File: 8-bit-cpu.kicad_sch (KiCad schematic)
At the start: 24 parts

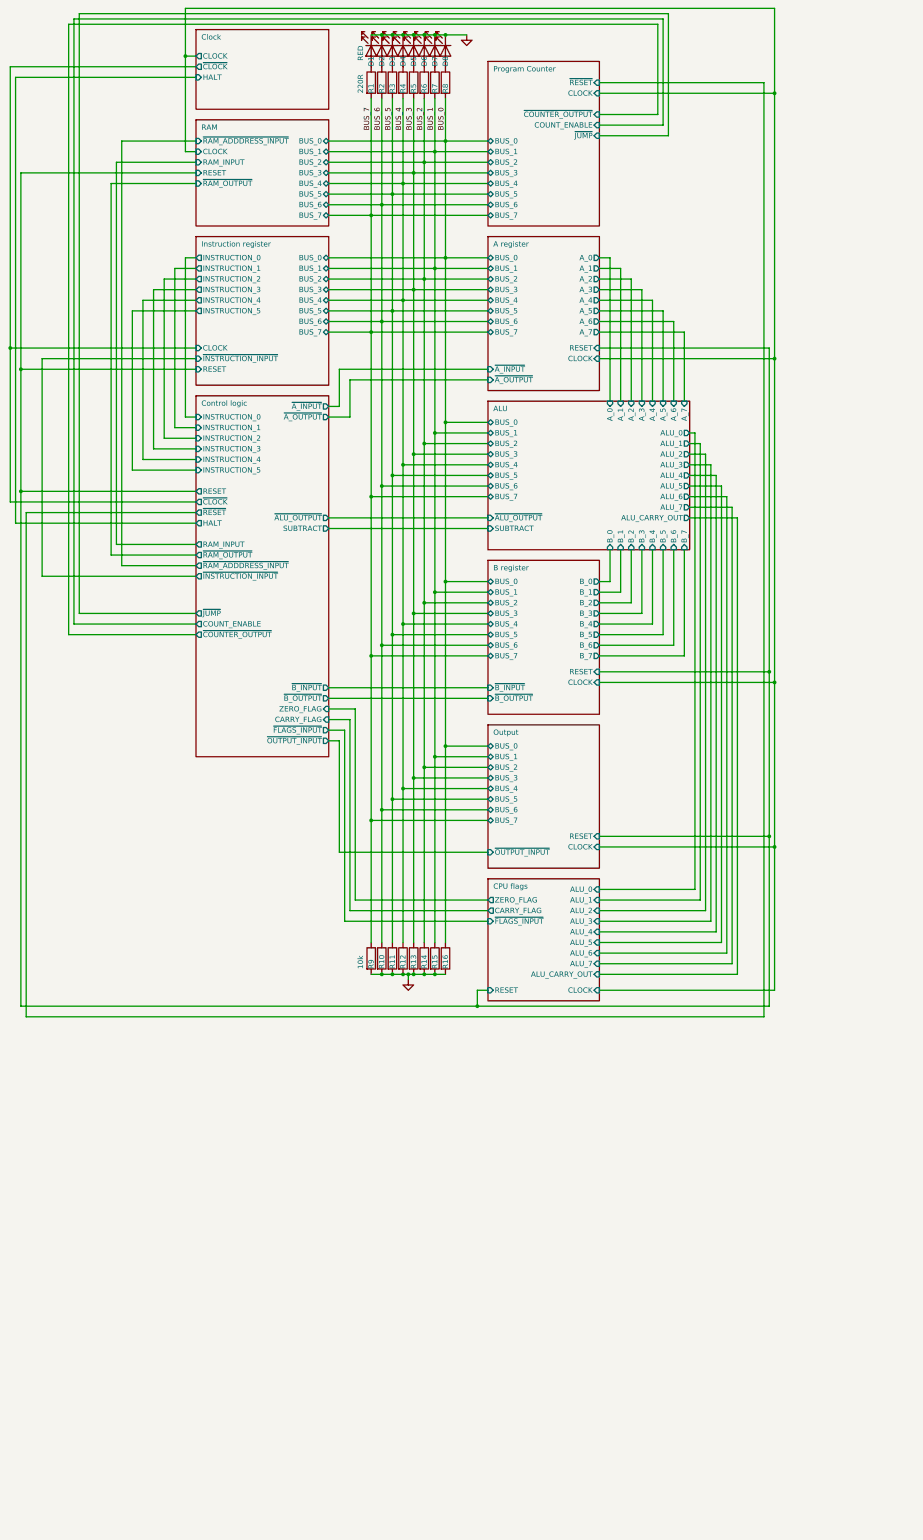
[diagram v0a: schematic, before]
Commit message: added stack and x register.  Added logic for stack_address so ram address 7 gets passes and ram address 8 is high
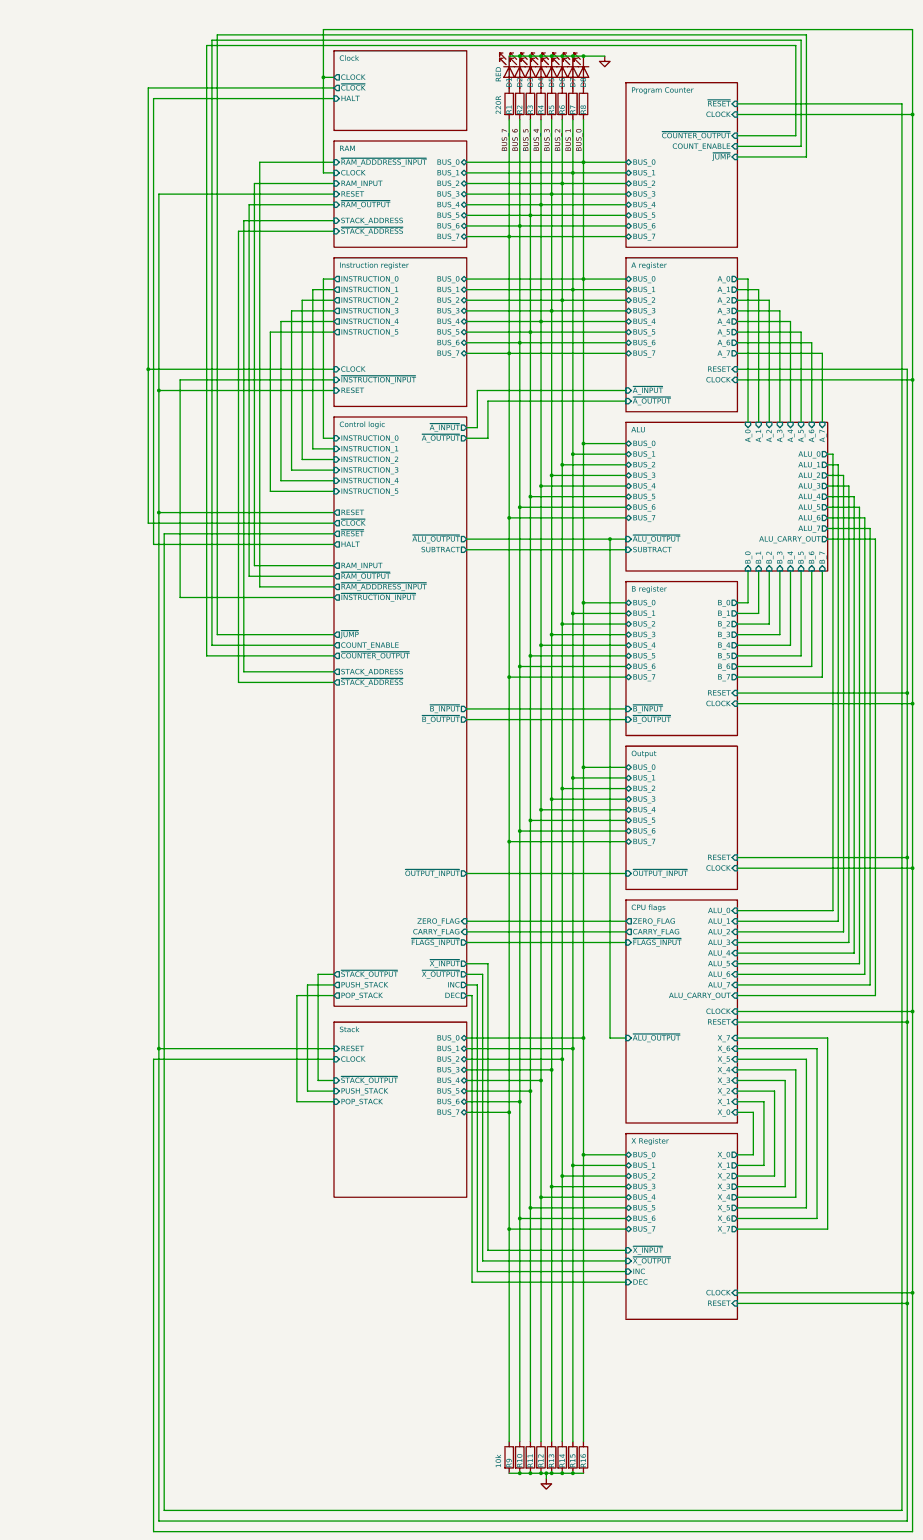
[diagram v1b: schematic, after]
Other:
- added sheet Stack (stack.kicad_sch)
- added sheet X Register (x-register.kicad_sch)
- sheet CPU flags ports: added X_0, X_1, X_2, X_3, X_4, X_5, X_6, X_7, ~{ALU_OUTPUT}; removed none
- sheet Control logic ports: added DEC, INC, POP_STACK, PUSH_STACK, STACK_ADDRESS, ~{STACK_ADDRESS}, ~{STACK_OUTPUT}, ~{X_INPUT}, ~{X_OUTPUT}; removed none
- sheet RAM ports: added STACK_ADDRESS, ~{STACK_ADDRESS}; removed none
- moved on the sheet: D1, D2, D3, D4, D5, D6, D7, D8, R1, R10, R11, R12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

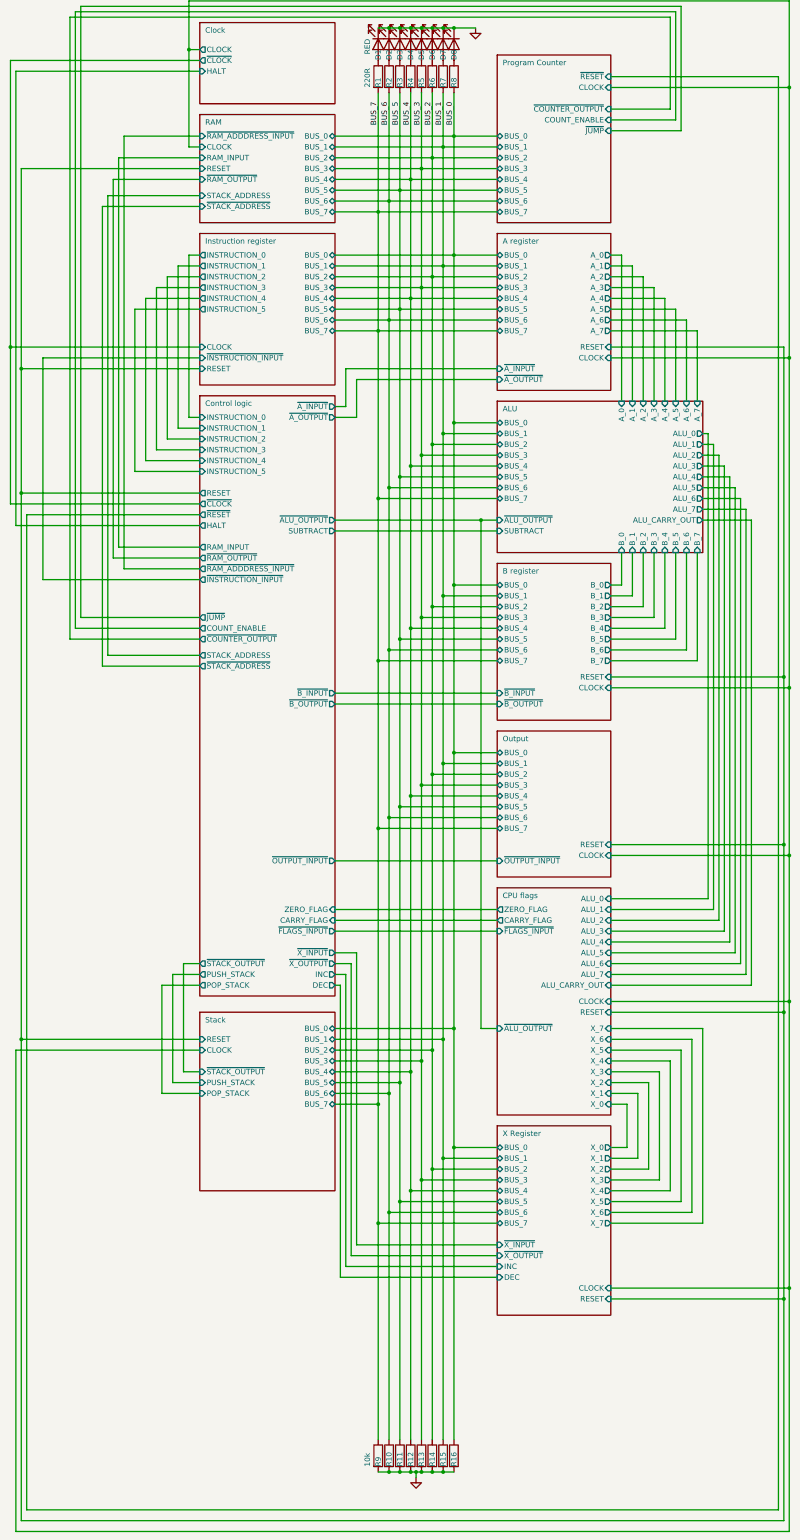
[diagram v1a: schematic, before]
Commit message: changed symbols
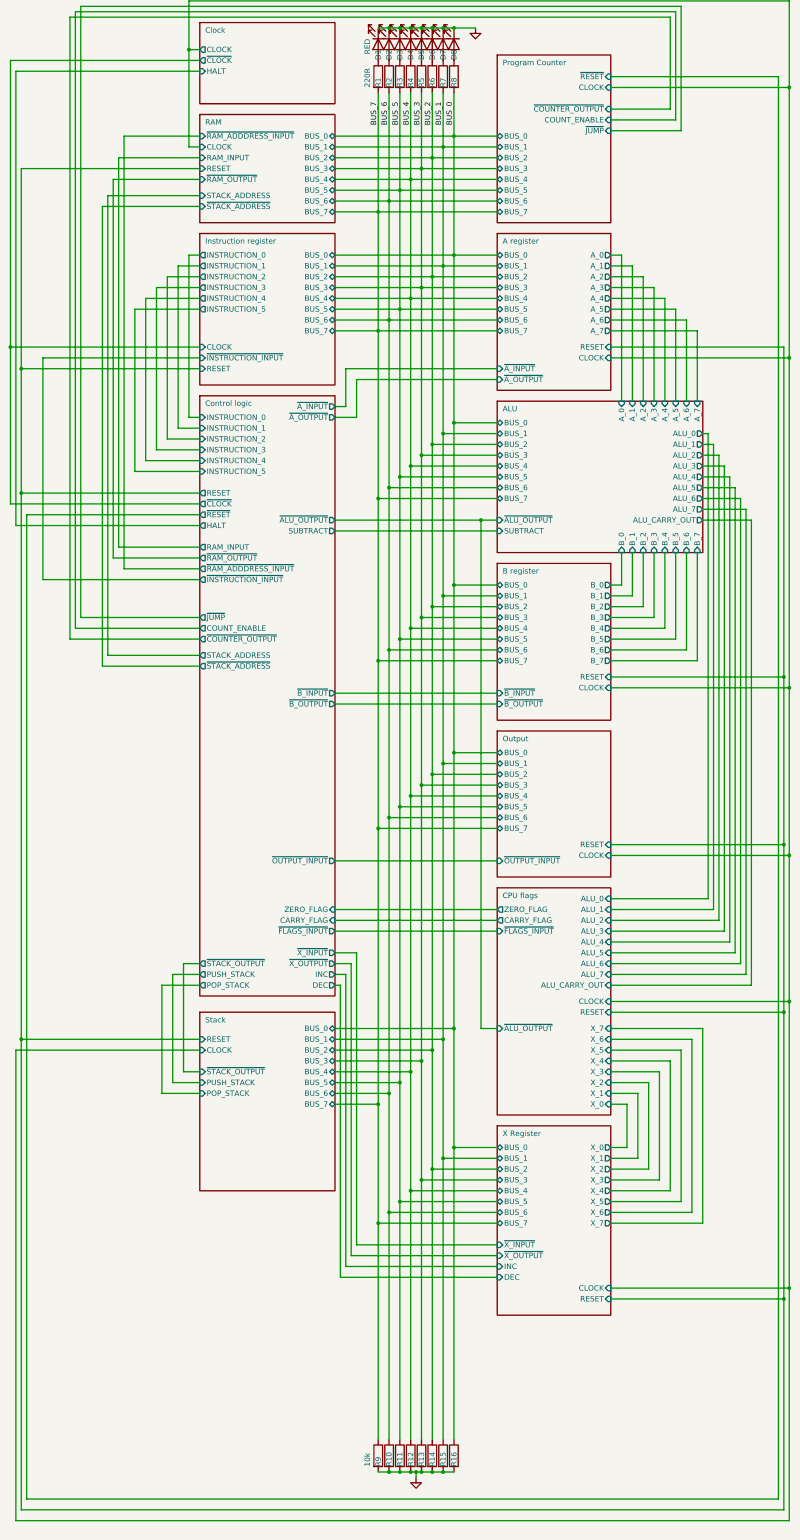
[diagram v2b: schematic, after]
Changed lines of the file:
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@@
     (stroke (width 0) (type default) (color 0 0 255 1))
   )
-  (wire (pts (xy 49.53 261.62) (xy 49.53 374.65))
+  (wire (pts (xy 49.53 261.62) (xy 49.53 372.11))
     (stroke (width 0) (type default) (color 255 0 0 1))
   )
@@
     (stroke (width 0) (type default) (color 255 0 0 1))
   )
-  (wire (pts (xy 228.6 322.58) (xy 228.6 374.65))
+  (wire (pts (xy 228.6 322.58) (xy 228.6 372.11))
     (stroke (width 0) (type default) (color 255 0 0 1))
   )
@@
     (stroke (width 0) (type default) (color 0 0 255 1))
   )
-  (wire (pts (xy 229.87 320.04) (xy 229.87 377.19))
+  (wire (pts (xy 229.87 320.04) (xy 229.87 374.65))
     (stroke (width 0) (type default) (color 255 0 0 1))
   )
@@
     (stroke (width 0) (type default) (color 0 0 255 1))
   )
-  (wire (pts (xy 48.26 264.16) (xy 48.26 377.19))
+  (wire (pts (xy 48.26 264.16) (xy 48.26 374.65))
     (stroke (width 0) (type default) (color 255 0 0 1))
   )
@@
     (stroke (width 0) (type default) (color 0 0 255 1))
   )
-  (wire (pts (xy 50.8 372.11) (xy 50.8 138.43))
+  (wire (pts (xy 50.8 369.57) (xy 50.8 138.43))
     (stroke (width 0) (type default) (color 255 0 0 1))
   )
@@
     (stroke (width 0) (type default))
   )
-  (wire (pts (xy 49.53 374.65) (xy 228.6 374.65))
+  (wire (pts (xy 49.53 372.11) (xy 228.6 372.11))
     (stroke (width 0) (type default) (color 255 0 0 1))
   )
@@
     (stroke (width 0) (type default))
   )
-  (wire (pts (xy 227.33 372.11) (xy 50.8 372.11))
+  (wire (pts (xy 227.33 369.57) (xy 50.8 369.57))
     (stroke (width 0) (type default) (color 255 0 0 1))
   )
@@
     (stroke (width 0) (type default) (color 0 0 255 1))
   )
-  (wire (pts (xy 227.33 35.56) (xy 227.33 372.11))
+  (wire (pts (xy 227.33 35.56) (xy 227.33 369.57))
     (stroke (width 0) (type default) (color 255 0 0 1))
   )
@@
     (stroke (width 0) (type default))
   )
-  (wire (pts (xy 48.26 377.19) (xy 229.87 377.19))
-    (stroke (width 0) (type default) (color 255 0 0 1))
-  )
+  (wire (pts (xy 48.26 374.65) (xy 229.87 374.65))
+    (stroke (width 0) (type default) (color 255 0 0 1))
+  )

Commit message: trying to solve issues
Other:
- sheet Control logic ports: added X_INPUT; removed ~{X_INPUT}
- sheet X Register ports: added X_INPUT; removed ~{X_INPUT}
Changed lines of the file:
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@@
       (effects (font (size 1.27 1.27)) (justify left))
     )
-    (pin "~{X_INPUT}" input (at 161.29 309.88 180)
+    (pin "X_INPUT" input (at 161.29 309.88 180)
       (effects (font (size 1.27 1.27)) (justify left))
     )
@@
     (instances
       (project "8-bit-cpu"
-        (path "/100bb8d1-c3d6-4e1f-87b6-72e4e187243c" (page "19"))
+        (path "/100bb8d1-c3d6-4e1f-87b6-72e4e187243c" (page "20"))
       )
     )
@@
     (instances
       (project "8-bit-cpu"
-        (path "/100bb8d1-c3d6-4e1f-87b6-72e4e187243c" (page "18"))
+        (path "/100bb8d1-c3d6-4e1f-87b6-72e4e187243c" (page "19"))
       )
     )
@@
     (instances
       (project "8-bit-cpu"
-        (path "/100bb8d1-c3d6-4e1f-87b6-72e4e187243c" (page "20"))
+        (path "/100bb8d1-c3d6-4e1f-87b6-72e4e187243c" (page "21"))
       )
     )
@@
       (effects (font (size 1.27 1.27)) (justify right))
     )
-    (pin "~{X_INPUT}" output (at 123.19 241.3 0)
-      (effects (font (size 1.27 1.27)) (justify right))
-    )
+    (pin "X_INPUT" output (at 123.19 241.3 0)
+      (effects (font (size 1.27 1.27)) (justify right))
+    )

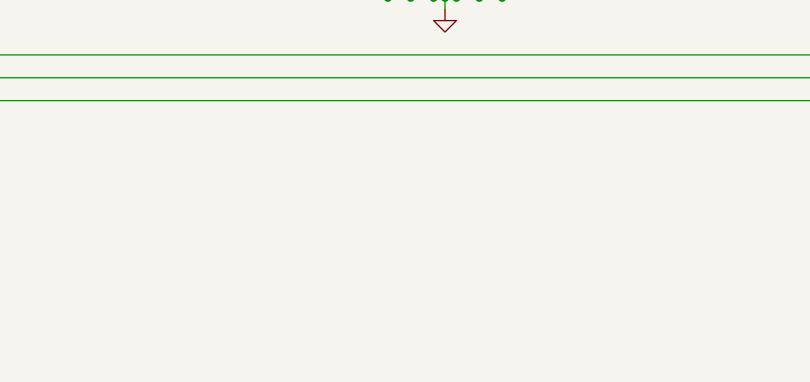
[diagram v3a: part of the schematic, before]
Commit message: added breadboard layout
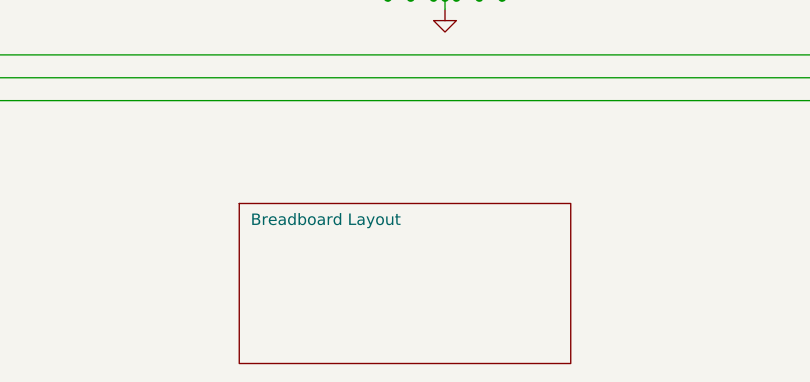
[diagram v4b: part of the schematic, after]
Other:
- added sheet Breadboard Layout (breadboard-layout.kicad_sch)
